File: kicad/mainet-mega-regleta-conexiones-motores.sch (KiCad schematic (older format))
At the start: 5 parts, among them J93 Regleta de Conexiones, J94 Screw_Terminal_01x15, J95 Conn_01x01_Male, J96 Conn_01x01_Male, J97 Conn_01x01_Male

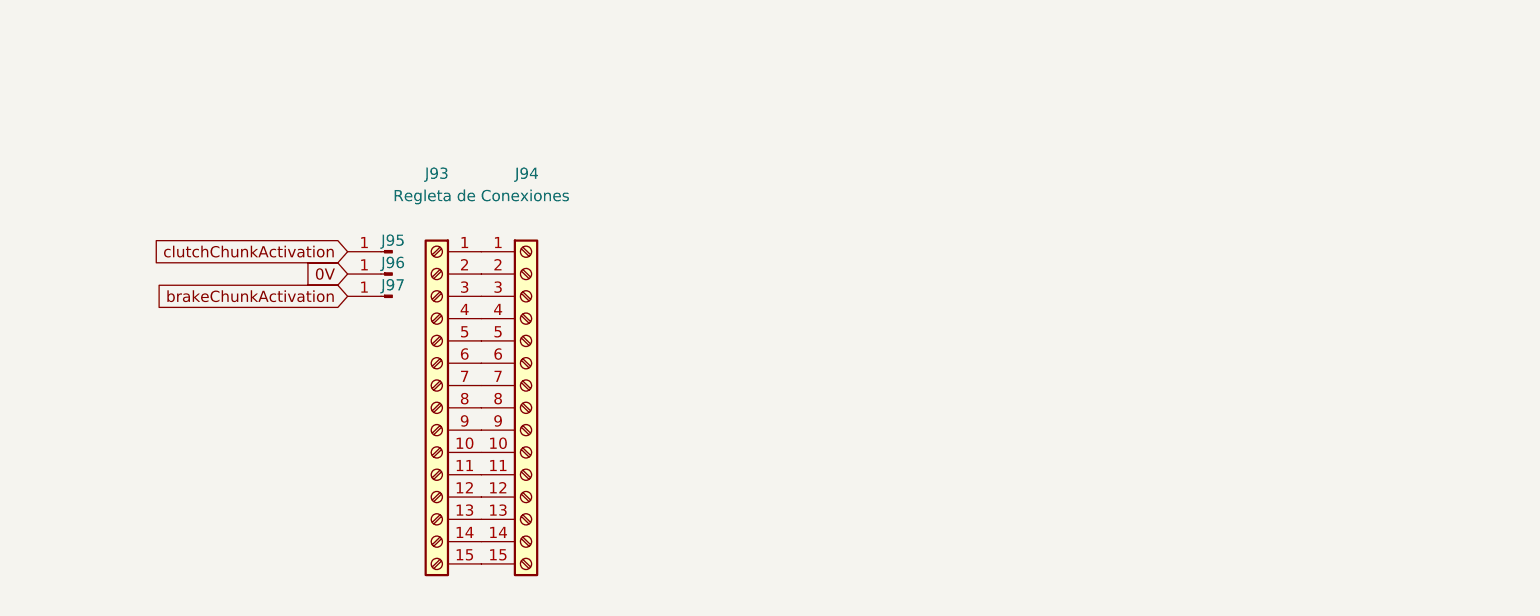
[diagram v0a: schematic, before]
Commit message: KICAD: Actualizar .sch regleta conexión embragues
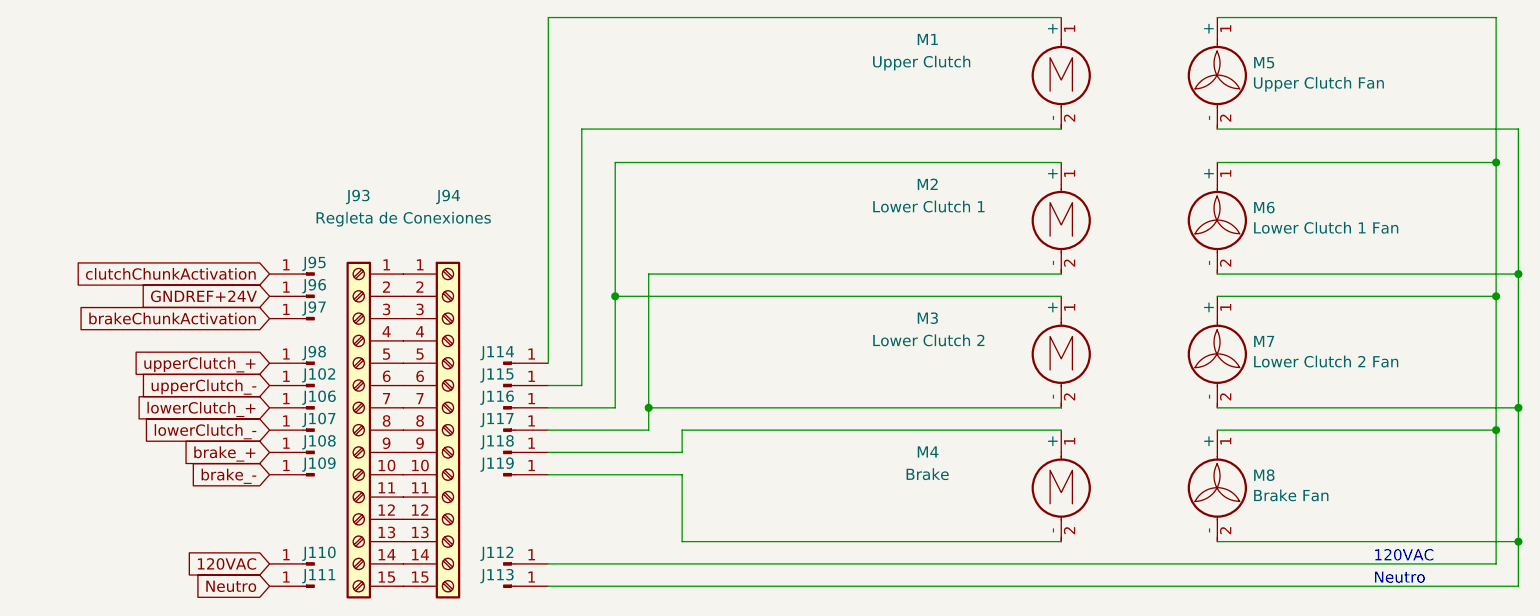
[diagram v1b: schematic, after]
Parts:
- added J102, J106, J107, J108, J109, J110, J111, J112, J113, J114, J115, J116, J117, J118, J119, J98: Conn_01x01_Male, symbol Connector:Conn_01x01_Male
- added M1: Upper Clutch, symbol Motor:Motor_DC
- added M2: Lower Clutch 1, symbol Motor:Motor_DC
- added M3: Lower Clutch 2, symbol Motor:Motor_DC
- added M4: Brake, symbol Motor:Motor_DC
- added M5: Upper Clutch Fan, symbol Motor:Fan
- added M6: Lower Clutch 1 Fan, symbol Motor:Fan
- added M7: Lower Clutch 2 Fan, symbol Motor:Fan
- added M8: Brake Fan, symbol Motor:Fan
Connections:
- net 0V renamed GNDREF+24V
- new net: J112.1 (Pin_1), M5.1 (+), M6.1 (+), M7.1 (+), M8.1 (+)
- new net: J113.1 (Pin_1), M5.2 (-), M6.2 (-), M7.2 (-), M8.2 (-)
- new net: J114.1 (Pin_1), M1.1 (+)
- new net: J115.1 (Pin_1), M1.2 (-)
- new net: J116.1 (Pin_1), M2.1 (+), M3.1 (+)
- new net: J117.1 (Pin_1), M2.2 (-), M3.2 (-)
- new net: J118.1 (Pin_1), M4.1 (+)
- new net: J119.1 (Pin_1), M4.2 (-)
- new net 120VAC: J110.1 (Pin_1)
- new net Neutro: J111.1 (Pin_1)
- new net brake_+: J108.1 (Pin_1)
- new net brake_-: J109.1 (Pin_1)
- new net lowerClutch_+: J106.1 (Pin_1)
- new net lowerClutch_-: J107.1 (Pin_1)
- new net upperClutch_+: J98.1 (Pin_1)
- new net upperClutch_-: J102.1 (Pin_1)
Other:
- note added: "120VAC"
- note added: "Neutro"
- moved on the sheet: J93, J94, J95, J96, J97

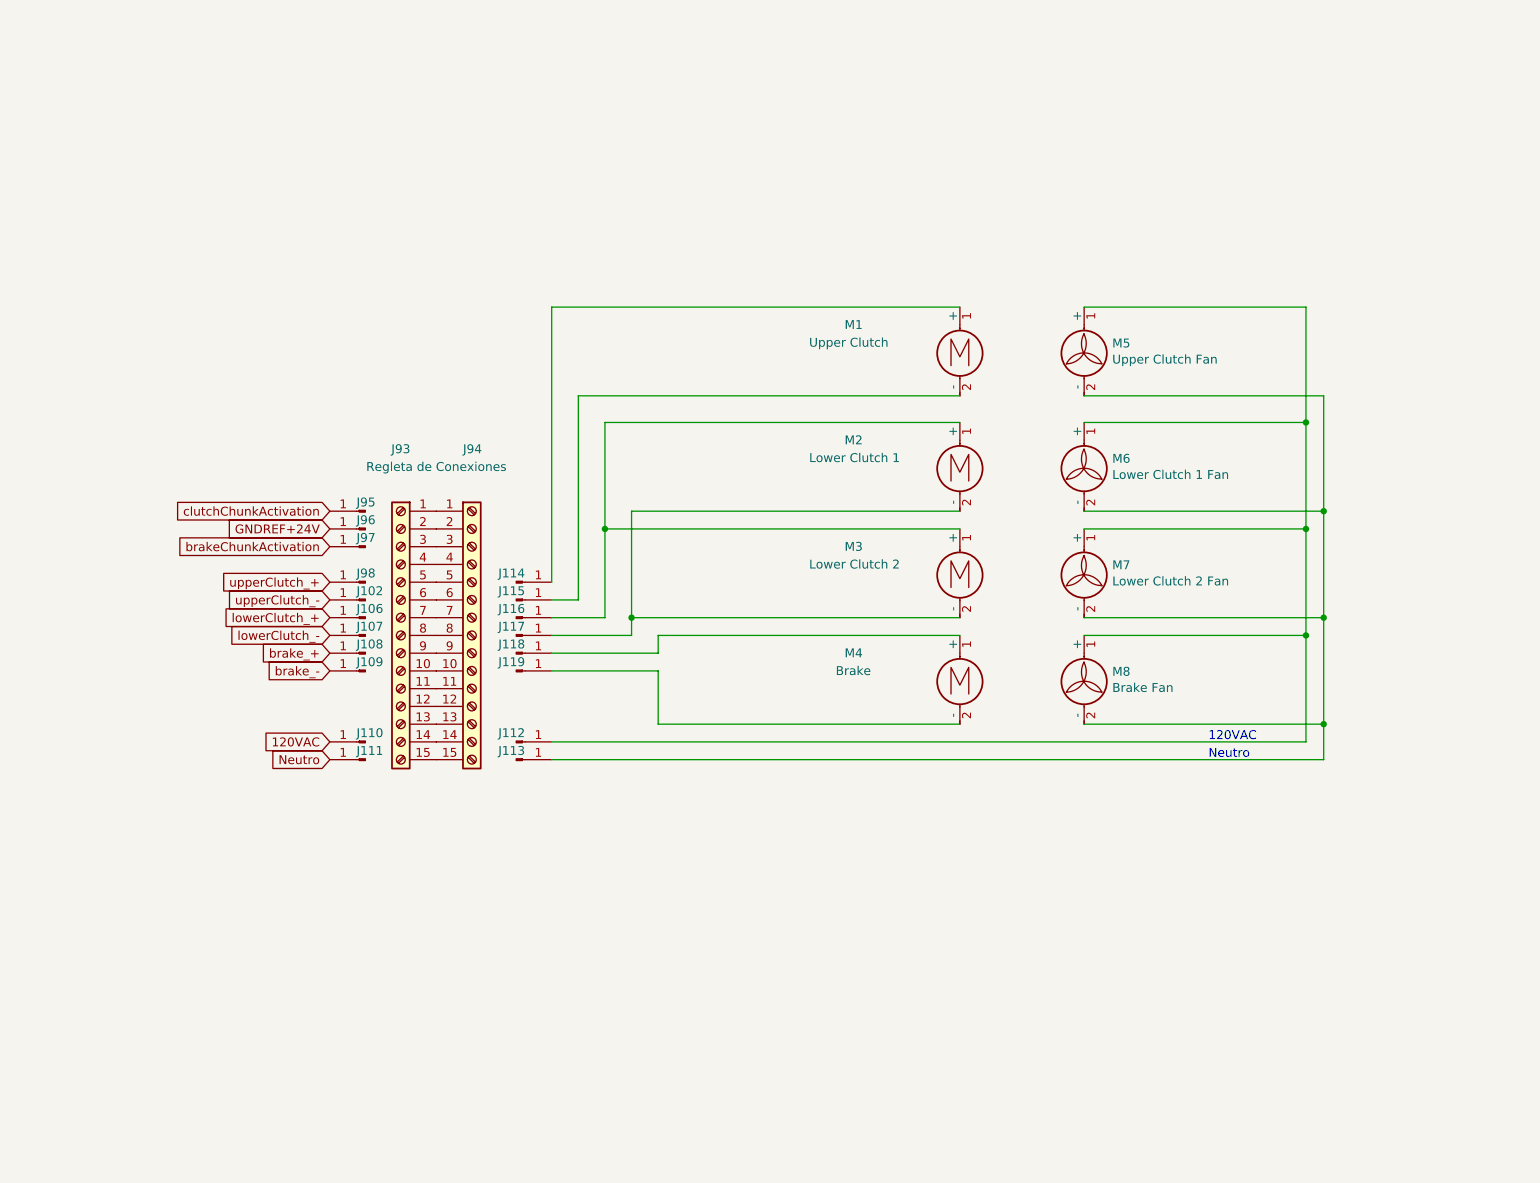
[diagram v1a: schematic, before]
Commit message: KICAD: Actualizar sch de la regleta de conexiones
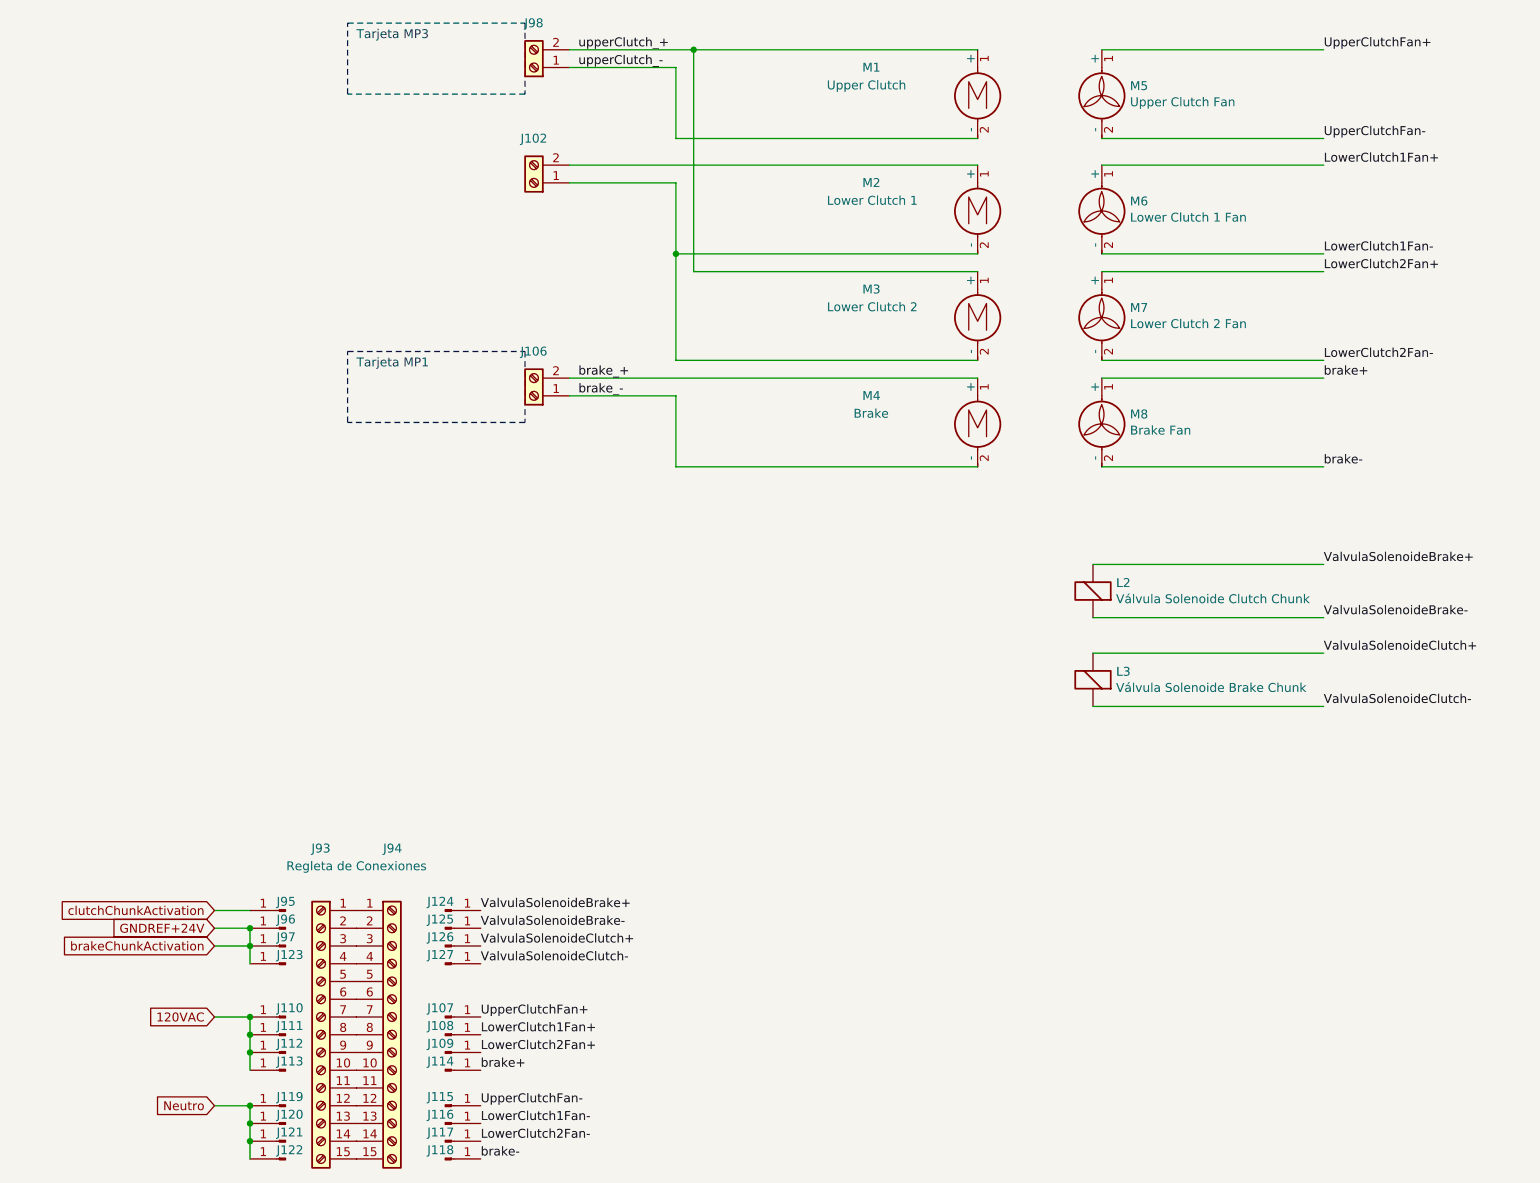
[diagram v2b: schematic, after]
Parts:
- removed J102, J106, J98: Conn_01x01_Male, symbol Connector:Conn_01x01_Male
- added J102, J106, J98: Screw_Terminal_01x02, symbol Connector:Screw_Terminal_01x02
- added J120, J121, J122, J123, J124, J125, J126, J127: Conn_01x01_Male, symbol Connector:Conn_01x01_Male
- added L2: Válvula Solenoide Clutch Chunk, symbol Device:Electromagnetic_Actor
- added L3: Válvula Solenoide Brake Chunk, symbol Device:Electromagnetic_Actor
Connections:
- net brakeChunkActivation is gone; now on net GNDREF+24V: J97.1 (Pin_1)
- net 120VAC: now also J111.1 (Pin_1), J112.1 (Pin_1), J113.1 (Pin_1)
- net GNDREF+24V: now also J123.1 (Pin_1)
- net Neutro: now also J119.1 (Pin_1), J120.1 (Pin_1), J121.1 (Pin_1), J122.1 (Pin_1); no longer J111.1 (Pin_1)
- net brake_+: now also M4.1 (+), J106.2 (Pin_2); no longer J108.1 (Pin_1)
- net brake_-: now also M4.2 (-), J106.1 (Pin_1); no longer J109.1 (Pin_1)
- net upperClutch_+: now also M1.1 (+), M3.1 (+), J98.2 (Pin_2)
- net upperClutch_-: now also M1.2 (-), J98.1 (Pin_1)
- net brake+: now reaches J114.1 (Pin_1)
- net brake+: now also M8.1 (+); no longer M1.1 (+)
- net UpperClutchFan-: now reaches J115.1 (Pin_1)
- net UpperClutchFan-: now also M5.2 (-); no longer M1.2 (-)
- net at M2.2 (-), M3.2 (-): now also J102.1 (Pin_1); no longer J117.1 (Pin_1)
- net brake-: now reaches J118.1 (Pin_1)
- net brake-: now also M8.2 (-); no longer M4.1 (+)
- net lowerClutch_- renamed UpperClutchFan+
- net UpperClutchFan+: now also M5.1 (+)
- new net: J102.2 (Pin_2), M2.1 (+)
- new net LowerClutch1Fan+: J108.1 (Pin_1), M6.1 (+)
- new net LowerClutch1Fan-: J116.1 (Pin_1), M6.2 (-)
- new net LowerClutch2Fan+: J109.1 (Pin_1), M7.1 (+)
- new net LowerClutch2Fan-: J117.1 (Pin_1), M7.2 (-)
- new net ValvulaSolenoideBrake+: J124.1 (Pin_1), L2.2 (+)
- new net ValvulaSolenoideBrake-: J125.1 (Pin_1), L2.1 (-)
- new net ValvulaSolenoideClutch+: J126.1 (Pin_1), L3.2 (+)
- new net ValvulaSolenoideClutch-: J127.1 (Pin_1), L3.1 (-)
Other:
- note added: "Tarjeta MP1"
- note added: "Tarjeta MP3"
- note removed: "120VAC"
- note removed: "Neutro"
- moved on the sheet: J110, J111, J112, J113, J93, J94, J95, J96, J97, M1, M2, M3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

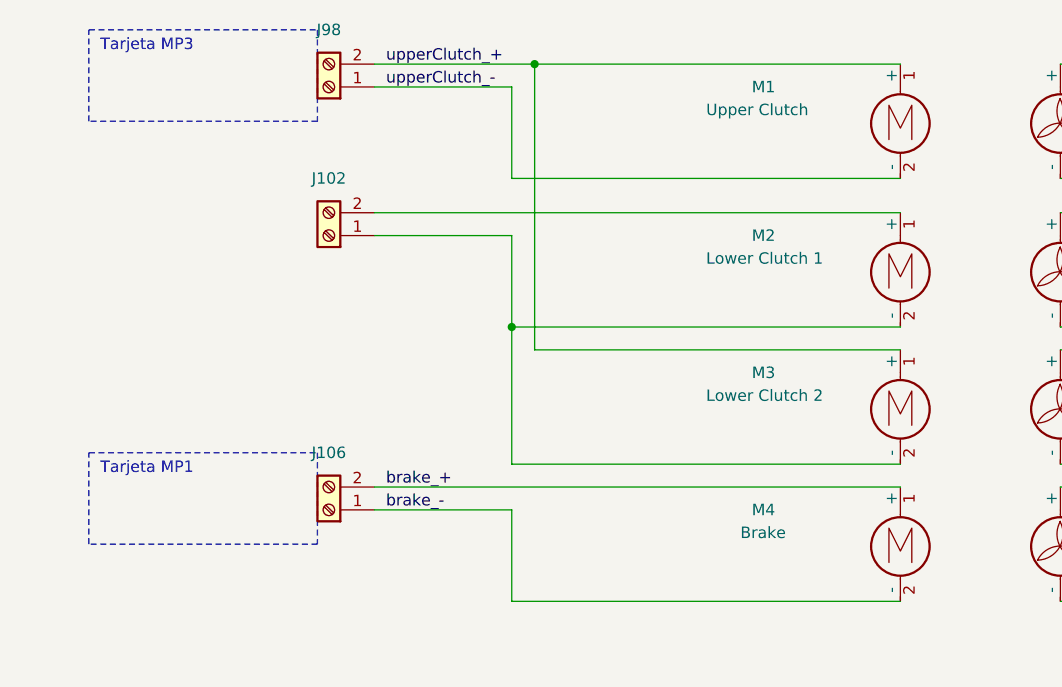
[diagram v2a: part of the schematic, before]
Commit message: KICAD: Actualizar .sch de la regleta de conexiones de embragues y freno
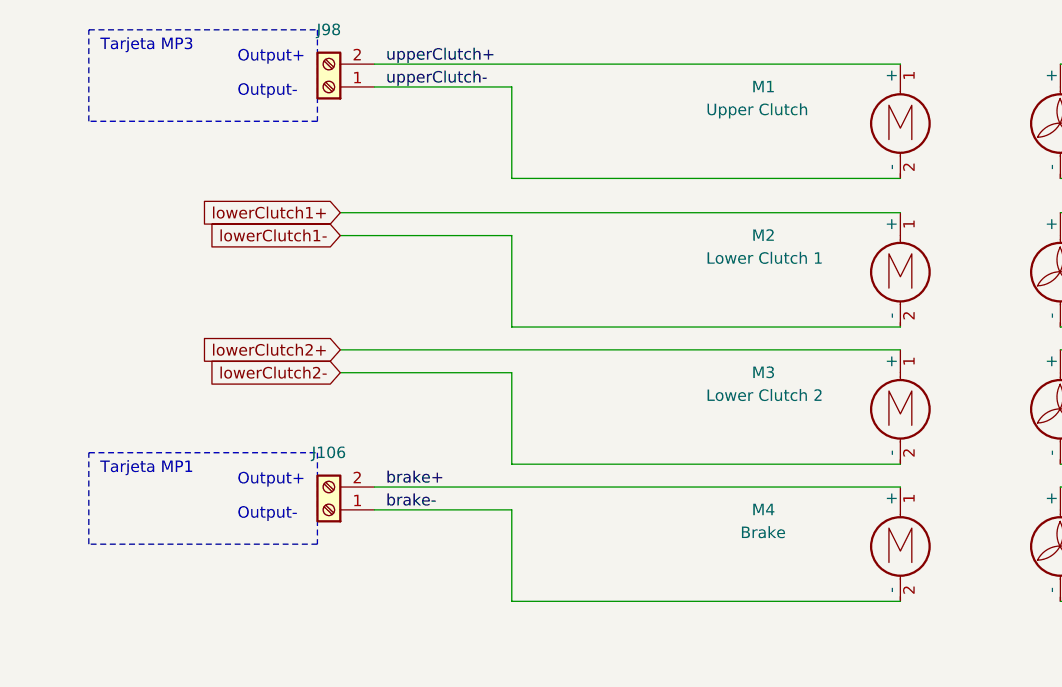
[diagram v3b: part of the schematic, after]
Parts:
- removed J102: Screw_Terminal_01x02, symbol Connector:Screw_Terminal_01x02
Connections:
- net brake_+ is gone; now on net brake+: J106.2 (Pin_2), M4.1 (+)
- net brake_- is gone; now on net brake-: J106.1 (Pin_1), M4.2 (-)
- net lowerClutch1-: now reaches M2.2 (-)
- net lowerClutch1-: no longer M3.2 (-)
- net lowerClutch1+: now reaches M2.1 (+)
- net upperClutch_+ renamed upperClutch+
- net upperClutch+: no longer M3.1 (+)
- net upperClutch_- renamed upperClutch-
- new net lowerClutch2+: M3.1 (+)
- new net lowerClutch2-: M3.2 (-)
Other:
- note added: "Output+"
- note added: "Output-"
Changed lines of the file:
@@
 Sheet 21 22
 Title "Regleta de conexiones"
-Date "2021-07-14"
+Date "2021-07-16"
 Rev "1.0"
 Comp ""
@@
 $EndComp
 Wire Wire Line
-	7050 850  5450 850
-Wire Wire Line
 	7050 1350 5350 1350
 Wire Wire Line
@@
 $EndComp
 $Comp
-L Connector:Screw_Terminal_01x02 J102
-U 1 1 60F33DCE
-P 4550 1600
-F 0 "J102" H 4550 1350 50  0000 C CNN
-F 1 "Screw_Terminal_01x02" H 4468 1366 50  0001 C CNN
-F 2 "" H 4550 1600 50  0001 C CNN
-F 3 "~" H 4550 1600 50  0001 C CNN
-	1    4550 1600
-	-1   0    0    1
-$EndComp
-$Comp
 L Connector:Screw_Terminal_01x02 J106
 U 1 1 60F38B9C
@@
 $EndComp
 Wire Wire Line
-	4750 1500 7050 1500
-Wire Wire Line
 	4750 2700 7050 2700
 Wire Wire Line
@@
 Wire Wire Line
 	5350 2000 7050 2000
-Wire Wire Line
-	4750 1600 5350 1600
 Wire Wire Line
 	5350 2600 7050 2600
@@
 	5350 2800 5350 3200
 Text Label 4800 850  0    50   ~ 0
-upperClutch_+
+upperClutch+
 Text Label 4800 950  0    50   ~ 0
-upperClutch_-
-Connection ~ 5350 2000
-Wire Wire Line
-	5350 2000 5350 2600
-Wire Wire Line
-	5450 2100 5450 850
-Wire Wire Line
-	5450 2100 7050 2100
-Connection ~ 5450 850
-Wire Wire Line
-	5450 850  4750 850
+upperClutch-
 Text Label 4800 2700 0    50   ~ 0
-brake_+
+brake+
 Text Label 4800 2800 0    50   ~ 0
-brake_-
+brake-
 Wire Notes Line
 	3500 700  4500 700
@@
 Text Label 9000 4550 0    50   ~ 0
 ValvulaSolenoideClutch-
+Text GLabel 4600 1500 0    50   Input ~ 0
+lowerClutch1+
+Text GLabel 4600 1600 0    50   Input ~ 0
+lowerClutch1-
+Wire Wire Line
+	4750 850  7050 850
+Text GLabel 4600 2100 0    50   Input ~ 0
+lowerClutch2+
+Text GLabel 4600 2200 0    50   Input ~ 0
+lowerClutch2-
+Wire Wire Line
+	4600 2100 7050 2100
+Wire Wire Line
+	4600 2200 5350 2200
+Wire Wire Line
+	5350 2200 5350 2600
+Wire Wire Line
+	4600 1500 7050 1500
+Wire Wire Line
+	4600 1600 5350 1600
+Text Notes 4150 850  0    50   ~ 0
+Output+
+Text Notes 4150 1000 0    50   ~ 0
+Output-
+Text Notes 4150 2700 0    50   ~ 0
+Output+
+Text Notes 4150 2850 0    50   ~ 0
+Output-
 $EndSCHEMATC
